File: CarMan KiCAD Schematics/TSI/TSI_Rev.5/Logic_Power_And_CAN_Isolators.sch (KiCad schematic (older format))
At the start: 3 parts

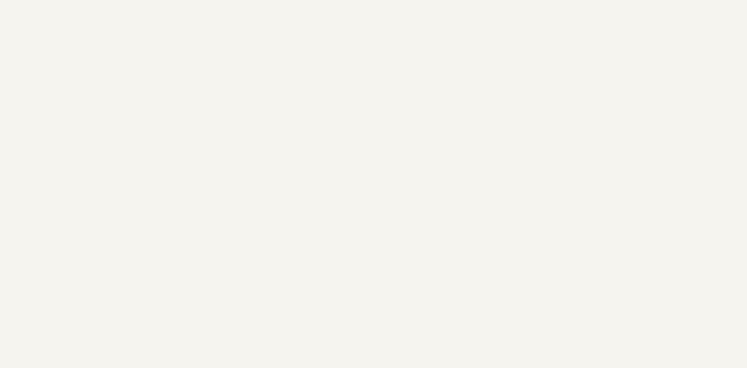
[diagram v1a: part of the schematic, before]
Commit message: Removed CAN Transciever from CAN & GLV Power, edited net listing on PCDC Circuit regarding Safety_Loop Iso and extraneous connector
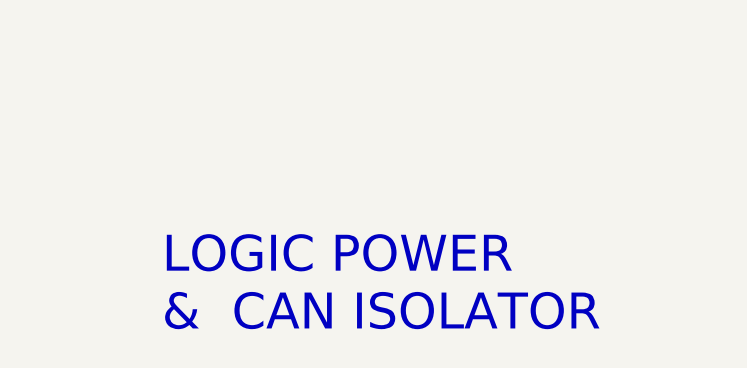
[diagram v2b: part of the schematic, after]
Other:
- note added: "LOGIC POWER \n& CAN ISOLATOR"
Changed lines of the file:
@@
 Text Label 9000 1300 2    50   ~ 0
 5V_ISO_RTN
+Text Notes 7400 7050 0    157  ~ 0
+LOGIC POWER  \n&  CAN ISOLATOR
 $EndSCHEMATC
